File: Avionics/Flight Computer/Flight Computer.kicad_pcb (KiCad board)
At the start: 4 copper layers, 50 x 40 mm, 177 parts, among them J1 ERF8-040-05.0-S-DV-K, J2 ERF8-040-05.0-S-DV-K, J3 473460001, J4 734120110, J5 0734120110, J6 734120110, U1 CC1310F128RGZR, U12 ATSAME70Q21A-AN, U2 CC1190RGVR, U3 CC2650F128RGZR, U4 CC2592RGVR, U5 MPU-9250, U7 LPS25HB, U8 MAX17243, U9 MAX-M8W, Y1 9HT11-32.768KDZB-T, Y2 7V-16.000MAHJ-T, Y3 XRCGB24M000F2P00R0, Y5 XRCGB24M000F2P00R0

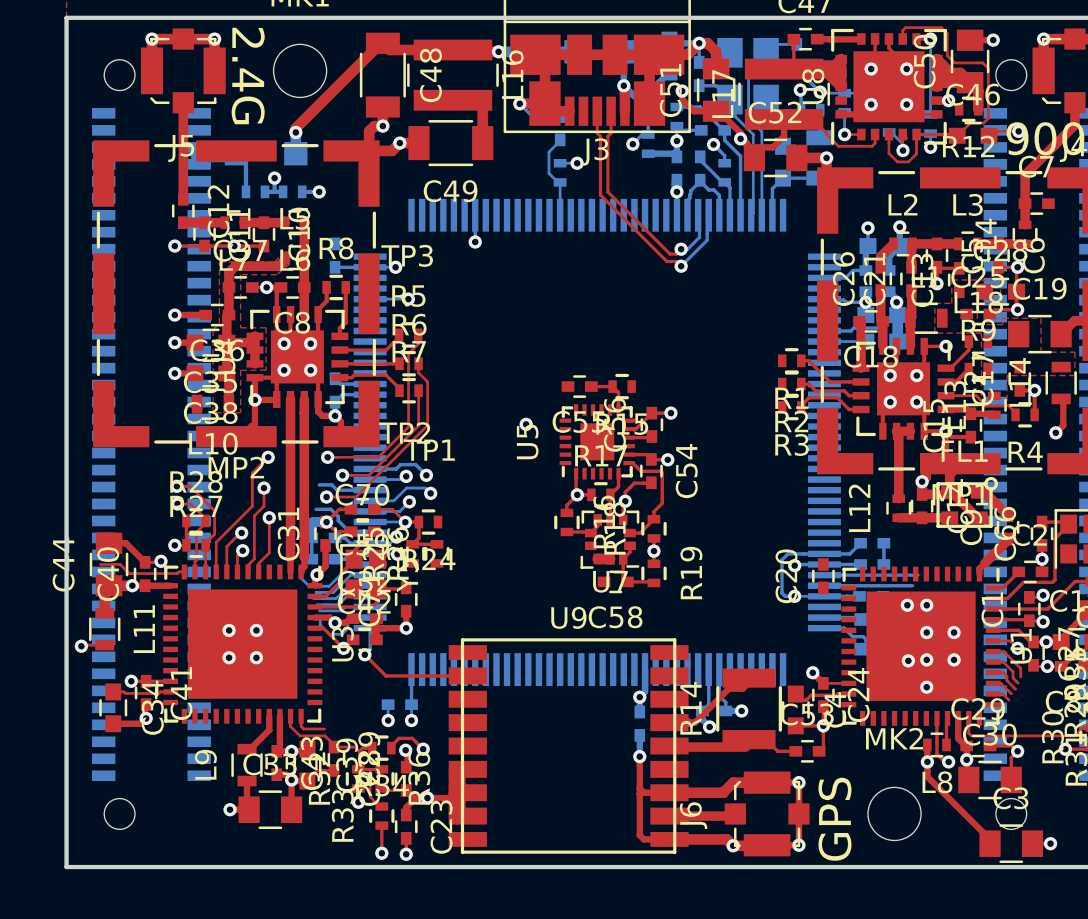
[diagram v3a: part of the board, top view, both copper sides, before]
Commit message: Continuing to route out MCU signals.
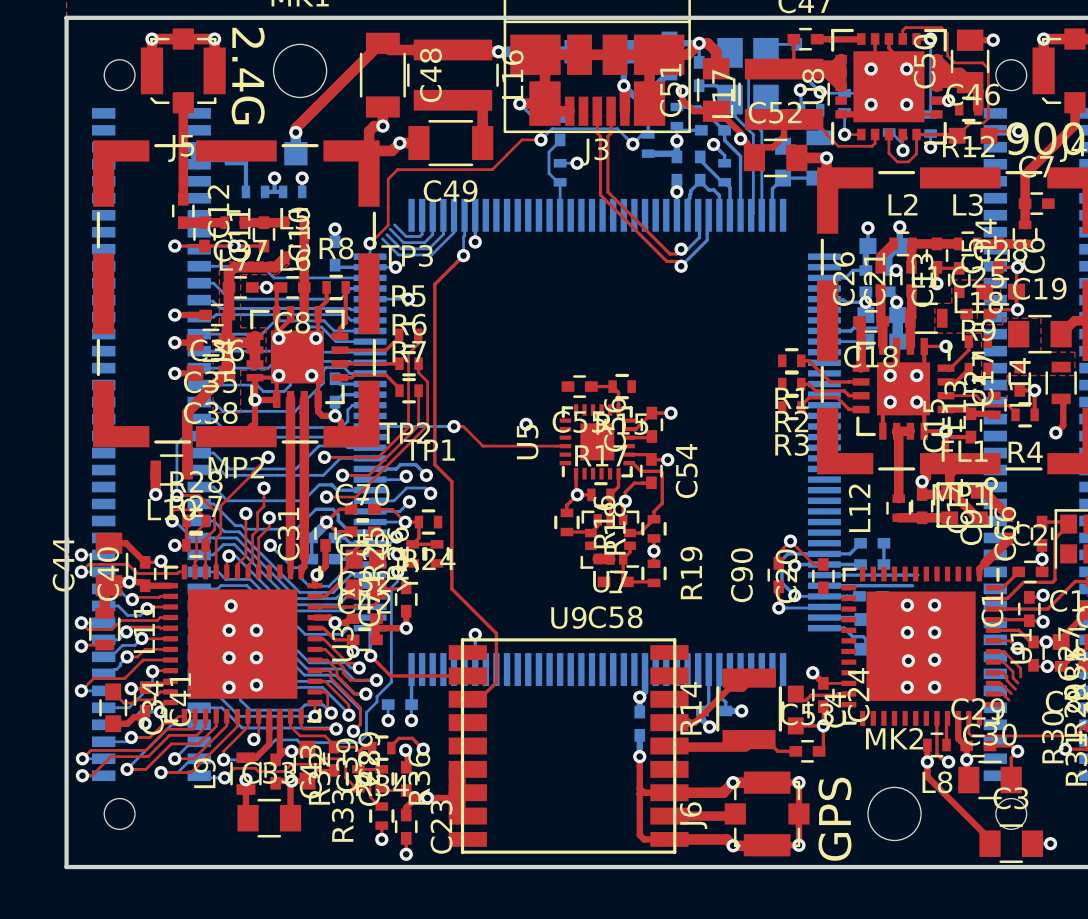
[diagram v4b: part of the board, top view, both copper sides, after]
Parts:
- added C90: 0.1u, Capacitors_SMD:C_0402, F.Cu at (83.5, 111.2)
- moved L10 3.66 mm to (55.0, 106.3)
- moved C43 0.40 mm to (59.9, 120.5)
- moved L9 0.40 mm to (58.5, 120.6)
- moved C33 0.40 mm to (59.6, 122.7)
- moved C41 0.30 mm to (53.7, 117.1)
- moved C77 0.10 mm to (62.6, 96.1)
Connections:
- J1 pad 11: Net-(J1-Pad11) -> /Connectors/PD9
- J1 pad 13: Net-(J1-Pad13) -> /Connectors/PC18
- J1 pad 15: Net-(J1-Pad15) -> /Connectors/PA28
- J1 pad 17: Net-(J1-Pad17) -> /Connectors/PD8
- J1 pad 19: Net-(J1-Pad19) -> /Connectors/PD15
- J1 pad 21: Net-(J1-Pad21) -> /Connectors/PB4
- J1 pad 23: Net-(J1-Pad23) -> /Connectors/PC17
- J1 pad 25: Net-(J1-Pad25) -> /Connectors/PA0
- J1 pad 27: Net-(J1-Pad27) -> /Connectors/PD10
- J1 pad 29: Net-(J1-Pad29) -> /Connectors/PC16
- J1 pad 31: Net-(J1-Pad31) -> /Connectors/PA1
- J1 pad 33: Net-(J1-Pad33) -> /Connectors/PD11
- J1 pad 35: Net-(J1-Pad35) -> /Connectors/PC14
- J1 pad 37: Net-(J1-Pad37) -> /Connectors/PC11
- J1 pad 39: Net-(J1-Pad39) -> /CPU-SDA
- J1 pad 41: Net-(J1-Pad41) -> /Connectors/PC10
- J1 pad 43: Net-(J1-Pad43) -> /Connectors/PB7
- J1 pad 45: Net-(J1-Pad45) -> /Connectors/PC9
- J1 pad 47: Net-(J1-Pad47) -> /Connectors/PC8
- J1 pad 49: Net-(J1-Pad49) -> /Connectors/PD16
- J1 pad 51: Net-(J1-Pad51) -> /CPU-SCK
- J1 pad 53: Net-(J1-Pad53) -> /Connectors/PC28
- J1 pad 54: Net-(J1-Pad54) -> /Connectors/PB6
- J1 pad 55: Net-(J1-Pad55) -> /Connectors/PD17
- J1 pad 56: Net-(J1-Pad56) -> /Connectors/2.4-DIO-7
- J1 pad 57: Net-(J1-Pad57) -> /Connectors/2.4-ADIO-30
- J1 pad 58: Net-(J1-Pad58) -> /Connectors/2.4-DIO-8
- J1 pad 59: Net-(J1-Pad59) -> /Connectors/2.4-ADIO-29
- J1 pad 60: Net-(J1-Pad60) -> /Connectors/2.4-DIO-9
- J1 pad 61: Net-(J1-Pad61) -> /Connectors/2.4-ADIO-28
- J1 pad 62: Net-(J1-Pad62) -> /Connectors/2.4-DIO-10
- J1 pad 63: Net-(J1-Pad63) -> /Connectors/2.4-ADIO-27
- J1 pad 64: Net-(J1-Pad64) -> /Connectors/2.4-DIO-11
- J1 pad 65: Net-(J1-Pad65) -> /Connectors/2.4-ADIO-26
- J1 pad 66: Net-(J1-Pad66) -> /Connectors/2.4-DIO-12
- J1 pad 67: Net-(J1-Pad67) -> /Connectors/2.4-ADIO-25
- J1 pad 68: Net-(J1-Pad68) -> /Connectors/2.4-DIO-13
- J1 pad 69: Net-(J1-Pad69) -> /Connectors/2.4-ADIO-24
- J1 pad 70: Net-(J1-Pad70) -> /Connectors/2.4-DIO-14
- J1 pad 71: Net-(J1-Pad71) -> /Connectors/2.4-ADIO-23
- J1 pad 72: Net-(J1-Pad72) -> /Connectors/2.4-DIO-15
- J1 pad 73: Net-(J1-Pad73) -> /Connectors/2.4-DIO-18
- J1 pad 74: Net-(J1-Pad74) -> /2.4-TMSC
- J1 pad 75: Net-(J1-Pad75) -> /Connectors/2.4-DIO-19
- J1 pad 76: Net-(J1-Pad76) -> /2.4-TCKC
- J1 pad 77: Net-(J1-Pad77) -> /Connectors/2.4-DIO-20
- J1 pad 78: Net-(J1-Pad78) -> /Connectors/2.4-DIO-16
- J1 pad 79: Net-(J1-Pad79) -> /2.4_RESET_EXT
- J1 pad 80: Net-(J1-Pad80) -> /Connectors/2.4-DIO-17
- J1 pad 9: Net-(J1-Pad9) -> /Connectors/PB5
- U12 pad 100: /GNC_Processor/PC16 -> /Connectors/PC16
- U12 pad 101: /GNC_Processor/PD10 -> /Connectors/PD10
- U12 pad 103: /GNC_Processor/PC17 -> /Connectors/PC17
- U12 pad 105: /GNC_Processor/PB4 -> /Connectors/PB4
- U12 pad 106: /GNC_Processor/PD15 -> /Connectors/PD15
- U12 pad 109: /GNC_Processor/PB5 -> /Connectors/PB5
- U12 pad 110: /GNC_Processor/PD9 -> /Connectors/PD9
- U12 pad 111: /GNC_Processor/PC18 -> /Connectors/PC18
- U12 pad 112: /GNC_Processor/PA28 -> /Connectors/PA28
- U12 pad 113: /GNC_Processor/PD8 -> /Connectors/PD8
- U12 pad 74: /GNC_Processor/PD17 -> /Connectors/PD17
- U12 pad 76: /GNC_Processor/PC28 -> /Connectors/PC28
- U12 pad 78: /GNC_Processor/PD16 -> /Connectors/PD16
- U12 pad 79: /GNC_Processor/PB6 -> /Connectors/PB6
- U12 pad 82: /GNC_Processor/PC8 -> /Connectors/PC8
- U12 pad 86: /GNC_Processor/PC9 -> /Connectors/PC9
- U12 pad 89: /GNC_Processor/PB7 -> /Connectors/PB7
- U12 pad 90: /GNC_Processor/PC10 -> /Connectors/PC10
- U12 pad 94: /GNC_Processor/PC11 -> /Connectors/PC11
- U12 pad 97: /GNC_Processor/PC14 -> /Connectors/PC14
- U12 pad 98: /GNC_Processor/PD11 -> /Connectors/PD11
- U3 pad 12: /2.4 GHz Radio/DIO-7 -> /Connectors/2.4-DIO-7
- U3 pad 14: /2.4 GHz Radio/DIO-8 -> /Connectors/2.4-DIO-8
- U3 pad 15: /2.4 GHz Radio/DIO-9 -> /Connectors/2.4-DIO-9
- U3 pad 16: /2.4 GHz Radio/DIO-10 -> /Connectors/2.4-DIO-10
- U3 pad 17: /2.4 GHz Radio/DIO-11 -> /Connectors/2.4-DIO-11
- U3 pad 18: /2.4 GHz Radio/DIO-12 -> /Connectors/2.4-DIO-12
- U3 pad 19: /2.4 GHz Radio/DIO-13 -> /Connectors/2.4-DIO-13
- U3 pad 20: /2.4 GHz Radio/DIO-14 -> /Connectors/2.4-DIO-14
- U3 pad 21: /2.4 GHz Radio/DIO-15 -> /Connectors/2.4-DIO-15
- U3 pad 26: /2.4 GHz Radio/DIO-16 -> /Connectors/2.4-DIO-16
- U3 pad 27: /2.4 GHz Radio/DIO-17 -> /Connectors/2.4-DIO-17
- U3 pad 28: /2.4 GHz Radio/DIO-18 -> /Connectors/2.4-DIO-18
- U3 pad 29: /2.4 GHz Radio/DIO-19 -> /Connectors/2.4-DIO-19
- U3 pad 30: /2.4 GHz Radio/DIO-20 -> /Connectors/2.4-DIO-20
- U3 pad 36: /2.4 GHz Radio/ADIO-23 -> /Connectors/2.4-ADIO-23
- U3 pad 37: /2.4 GHz Radio/ADIO-24 -> /Connectors/2.4-ADIO-24
- U3 pad 38: /2.4 GHz Radio/ADIO-25 -> /Connectors/2.4-ADIO-25
- U3 pad 39: /2.4 GHz Radio/ADIO-26 -> /Connectors/2.4-ADIO-26
- U3 pad 40: /2.4 GHz Radio/ADIO-27 -> /Connectors/2.4-ADIO-27
- U3 pad 41: /2.4 GHz Radio/ADIO-28 -> /Connectors/2.4-ADIO-28
- U3 pad 42: /2.4 GHz Radio/ADIO-29 -> /Connectors/2.4-ADIO-29
- U3 pad 43: /2.4 GHz Radio/ADIO-30 -> /Connectors/2.4-ADIO-30
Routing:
- net /GPS/GPS-Rx: track 0.00 -> 25.5 mm, vias 0 -> 1
- net /2.4 GHz Radio/VDDS_CC2650: track 11.6 -> 33.9 mm
- net /CPU_RESET_2.4: track 0.00 -> 19.0 mm, vias 0 -> 2
- net /2.4G-Rx: track 1.10 -> 18.9 mm, vias 1 -> 2
- net /Connectors/PB6: track 0.00 -> 17.1 mm, vias 0 -> 2
- net /GNC_Processor/VBUS_DETECT: track 1.81 -> 18.6 mm, vias 1 -> 3
- net /2.4 GHz Radio/VDDR_CC2650: track 6.24 -> 22.5 mm
- net /Connectors/2.4-ADIO-29: track 0.00 -> 14.4 mm, vias 0 -> 1
- net /Connectors/2.4-ADIO-27: track 0.00 -> 14.4 mm, vias 0 -> 1
- net /Connectors/2.4-ADIO-28: track 0.00 -> 13.0 mm, vias 0 -> 1
- net /Connectors/2.4-ADIO-30: track 0.00 -> 12.3 mm, vias 0 -> 1
- net /CPU-SDA: track 5.31 -> 16.8 mm
- net GND: track 225.3 -> 236.5 mm, vias 78 -> 85
- net /Connectors/2.4-ADIO-26: track 0.00 -> 10.8 mm, vias 0 -> 1
- net /Connectors/2.4-DIO-18: track 0.00 -> 9.90 mm, vias 0 -> 1
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
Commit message: Did some more routing
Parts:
- moved C20 0.75 mm to (85.7, 110.5)
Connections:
- J1 pad 1: Net-(J1-Pad1) -> /Connectors/PC19
- J1 pad 10: Net-(J1-Pad10) -> /Connectors/PA31
- J1 pad 2: Net-(J1-Pad2) -> /Connectors/PC21
- J1 pad 3: Net-(J1-Pad3) -> /Connectors/PA30
- J1 pad 4: Net-(J1-Pad4) -> /Connectors/PD6
- J1 pad 6: Net-(J1-Pad6) -> /Connectors/PC20
- J1 pad 8: Net-(J1-Pad8) -> /Connectors/PD7
- U12 pad 116: /GNC_Processor/PA30 -> /Connectors/PA30
- U12 pad 117: /GNC_Processor/PC19 -> /Connectors/PC19
- U12 pad 118: /GNC_Processor/PA31 -> /Connectors/PA31
- U12 pad 119: /GNC_Processor/PD7 -> /Connectors/PD7
- U12 pad 120: /GNC_Processor/PC20 -> /Connectors/PC20
- U12 pad 121: /GNC_Processor/PD6 -> /Connectors/PD6
- U12 pad 122: /GNC_Processor/PC21 -> /Connectors/PC21
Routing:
- net Net-(C57-Pad1): track 23.0 -> 90.2 mm, vias 7 -> 10
- net /Connectors/PD6: track 0.00 -> 29.2 mm
- net /Connectors/PC20: track 0.00 -> 28.7 mm
- net /Connectors/PD7: track 0.00 -> 28.7 mm
- net /Connectors/PC21: track 0.00 -> 28.1 mm, vias 0 -> 2
- net /Connectors/PA31: track 0.00 -> 23.7 mm
- net /900MHz Radio/VDDS_CC1310: track 12.4 -> 36.0 mm
- net /Connectors/PC19: track 0.00 -> 16.5 mm
- net /Connectors/PA30: track 0.00 -> 16.0 mm
- net /900MHz Radio/VDDR_CC1310: track 10.1 -> 25.5 mm
- net /GNC_Processor/GPS-~RESET: track 0.00 -> 12.1 mm, vias 0 -> 1
- net /Connectors/PB5: track 0.00 -> 11.5 mm
- net /Connectors/PD9: track 2.47 -> 13.0 mm
- net /Connectors/PC18: track 3.33 -> 13.4 mm
- net /Connectors/PA28: track 4.12 -> 14.1 mm
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
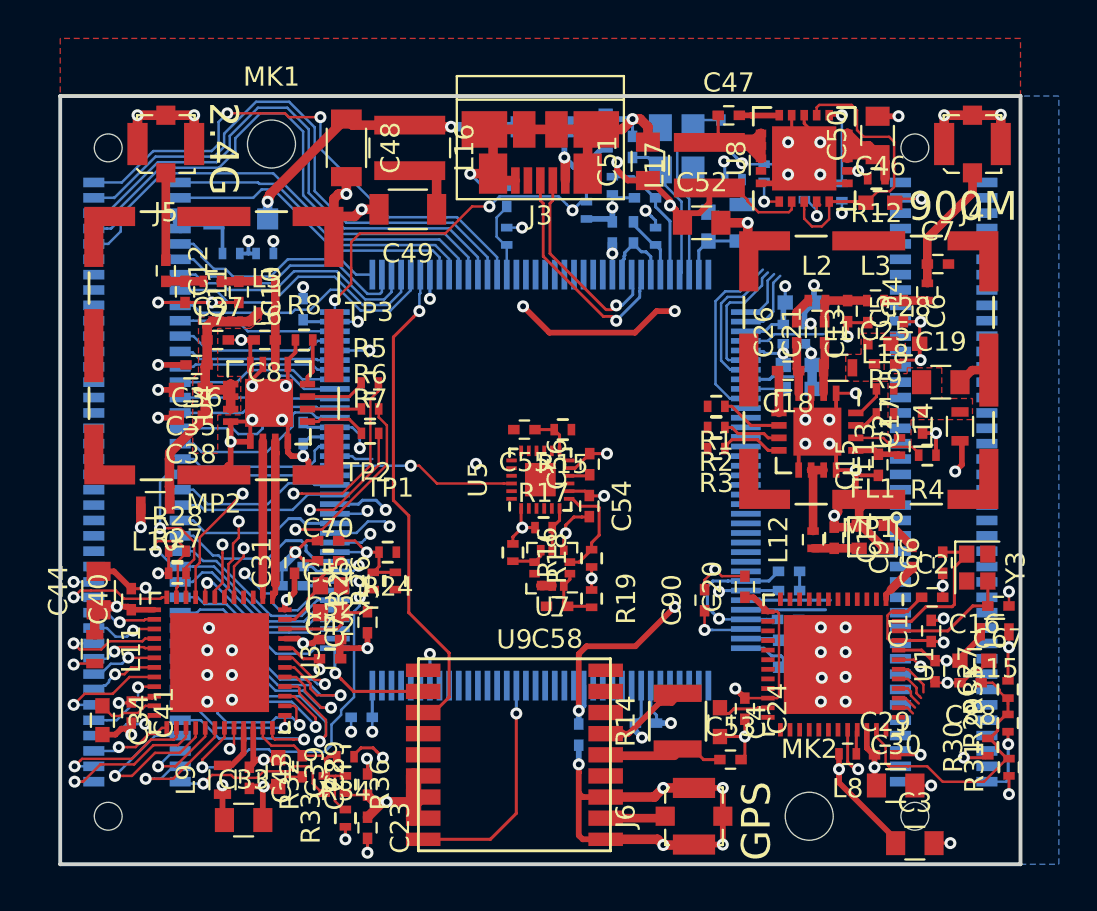
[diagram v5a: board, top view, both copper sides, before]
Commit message: Additional routing
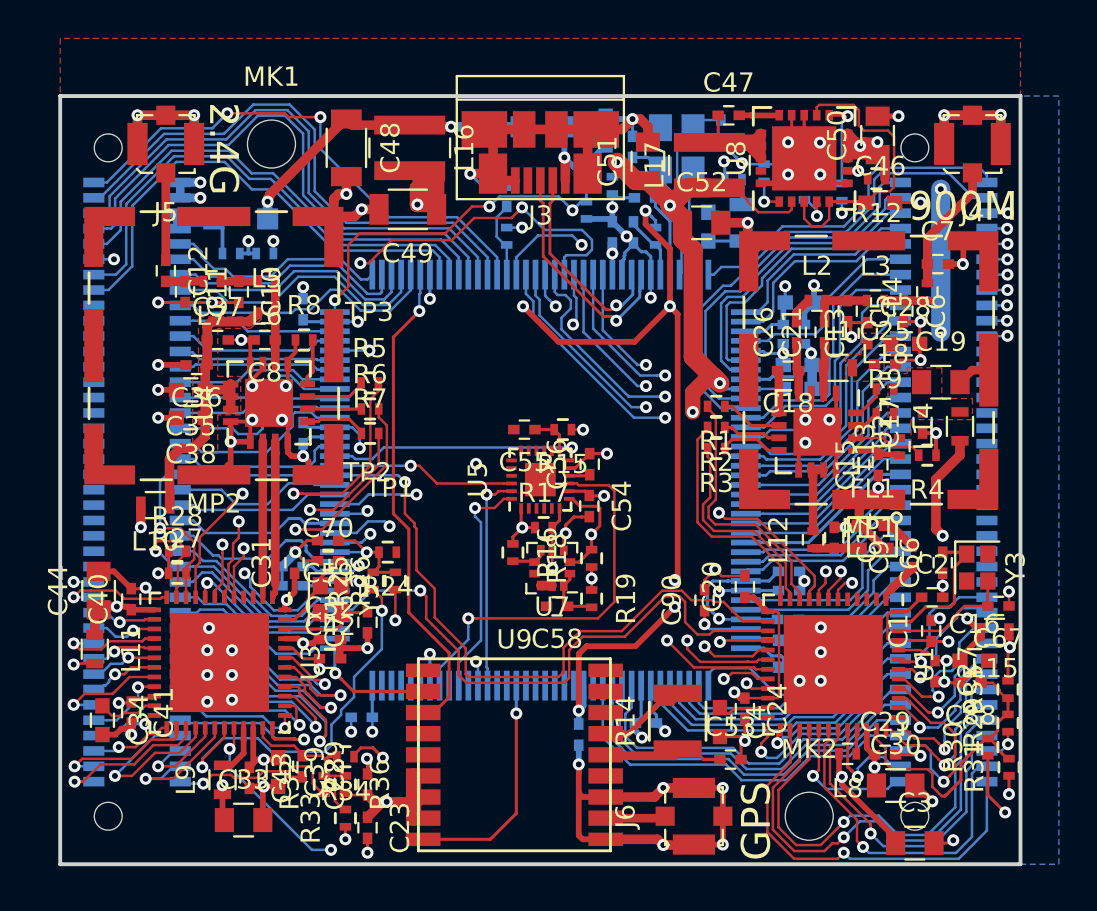
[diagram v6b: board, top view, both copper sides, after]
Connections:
- J1 pad 1: /Connectors/PC19 -> GND
- J1 pad 12: Net-(J1-Pad12) -> /Connectors/PA29
- J1 pad 14: Net-(J1-Pad14) -> /Connectors/PC19
- J1 pad 16: Net-(J1-Pad16) -> /Connectors/PA30
- J1 pad 3: /Connectors/PA30 -> GND
- J2 pad 1: Net-(J2-Pad1) -> /Connectors/PB13
- J2 pad 10: Net-(J2-Pad10) -> /Connectors/PD31
- J2 pad 11: Net-(J2-Pad11) -> /Connectors/PC25
- J2 pad 12: Net-(J2-Pad12) -> /Connectors/PE0
- J2 pad 13: Net-(J2-Pad13) -> /Connectors/PD1
- J2 pad 14: Net-(J2-Pad14) -> /Connectors/PC27
- J2 pad 15: Net-(J2-Pad15) -> /Connectors/PD2
- J2 pad 16: Net-(J2-Pad16) -> /Connectors/PC26
- J2 pad 17: Net-(J2-Pad17) -> /Connectors/PD3
- J2 pad 18: Net-(J2-Pad18) -> /Connectors/PC31
- J2 pad 19: Net-(J2-Pad19) -> /Connectors/PD4
- J2 pad 2: Net-(J2-Pad2) -> /Connectors/PE3
- J2 pad 20: Net-(J2-Pad20) -> /Connectors/PC30
- J2 pad 21: Net-(J2-Pad21) -> /Connectors/PD5
- J2 pad 22: Net-(J2-Pad22) -> /Connectors/PC29
- J2 pad 24: Net-(J2-Pad24) -> /Connectors/PC12
- J2 pad 26: Net-(J2-Pad26) -> /Connectors/PC15
- J2 pad 28: Net-(J2-Pad28) -> /Connectors/PC13
- J2 pad 3: Net-(J2-Pad3) -> /Connectors/PC0
- J2 pad 30: Net-(J2-Pad30) -> /Connectors/PB1
- J2 pad 32: Net-(J2-Pad32) -> /Connectors/PB0
- J2 pad 34: Net-(J2-Pad34) -> /Connectors/PA20
- J2 pad 36: Net-(J2-Pad36) -> /Connectors/PA19
- J2 pad 38: Net-(J2-Pad38) -> /Connectors/PA18
- J2 pad 4: Net-(J2-Pad4) -> /Connectors/PE2
- J2 pad 40: Net-(J2-Pad40) -> /Connectors/PA17
- J2 pad 42: Net-(J2-Pad42) -> /Connectors/PB2
- J2 pad 44: Net-(J2-Pad44) -> /Connectors/PE4
- J2 pad 46: Net-(J2-Pad46) -> /Connectors/PE5
- J2 pad 48: Net-(J2-Pad48) -> /Connectors/PB3
- J2 pad 5: Net-(J2-Pad5) -> /Connectors/PC22
- J2 pad 50: Net-(J2-Pad50) -> /Connectors/PA21
- J2 pad 52: Net-(J2-Pad52) -> /Connectors/PA22
- J2 pad 54: Net-(J2-Pad54) -> /Connectors/PC1
- J2 pad 55: Net-(J2-Pad55) -> /Connectors/900-ADIO-30
- J2 pad 56: Net-(J2-Pad56) -> /Connectors/PC2
- J2 pad 57: Net-(J2-Pad57) -> /Connectors/900-ADIO-29
- J2 pad 58: Net-(J2-Pad58) -> /Connectors/PC3
- J2 pad 59: Net-(J2-Pad59) -> /Connectors/900-ADIO-28
- J2 pad 6: Net-(J2-Pad6) -> /Connectors/PE1
- J2 pad 60: Net-(J2-Pad60) -> /Connectors/PC4
- J2 pad 61: Net-(J2-Pad61) -> /Connectors/900-ADIO-27
- J2 pad 62: Net-(J2-Pad62) -> /Connectors/PA13
- J2 pad 63: /Connectors/900-ADIO-30 -> /Connectors/900-ADIO-25
- J2 pad 64: Net-(J2-Pad64) -> /900-TCKC
- J2 pad 65: /Connectors/900-ADIO-29 -> /Connectors/900-ADIO-24
- J2 pad 66: Net-(J2-Pad66) -> /900-TMSC
- J2 pad 67: /Connectors/900-ADIO-28 -> /Connectors/900-ADIO-23
- J2 pad 68: Net-(J2-Pad68) -> /Connectors/PA16
- J2 pad 69: /Connectors/900-ADIO-26 -> /Connectors/900-DIO-18
- J2 pad 7: Net-(J2-Pad7) -> /Connectors/PC23
- J2 pad 70: Net-(J2-Pad70) -> /Connectors/PA23
- J2 pad 71: /Connectors/900-ADIO-23 -> /Connectors/900-DIO-17
- J2 pad 72: Net-(J2-Pad72) -> /Connectors/PD27
- J2 pad 73: /Connectors/900-ADIO-24 -> /Connectors/900-DIO-21
- J2 pad 74: Net-(J2-Pad74) -> /Connectors/PC7
- J2 pad 75: /Connectors/900-ADIO-25 -> /900_RESET_EXT
- J2 pad 76: Net-(J2-Pad76) -> /Connectors/900-ADIO-26
- J2 pad 77: /Connectors/900-ADIO-27 -> /Connectors/900-DIO-20
- J2 pad 78: Net-(J2-Pad78) -> /Connectors/900-DIO-22
- J2 pad 79: /900_RESET_EXT -> /Connectors/900-DIO-16
- J2 pad 8: Net-(J2-Pad8) -> /Connectors/PD0
- J2 pad 80: Net-(J2-Pad80) -> /Connectors/900-DIO-19
- J2 pad 9: Net-(J2-Pad9) -> /Connectors/PC24
- U1 pad 26: /900MHz Radio/DIO-16 -> /Connectors/900-DIO-16
- U1 pad 27: /900MHz Radio/DIO-17 -> /Connectors/900-DIO-17
- U1 pad 28: /900MHz Radio/DIO-18 -> /Connectors/900-DIO-18
- U1 pad 29: /900MHz Radio/DIO-19 -> /Connectors/900-DIO-19
- U1 pad 30: /900MHz Radio/DIO-20 -> /Connectors/900-DIO-20
- U1 pad 31: /900MHz Radio/DIO-21 -> /Connectors/900-DIO-21
- U1 pad 32: /900MHz Radio/DIO-22 -> /Connectors/900-DIO-22
- U12 pad 1: /GNC_Processor/PD0 -> /Connectors/PD0
- U12 pad 10: /GNC_Processor/PE3 -> /Connectors/PE3
- U12 pad 11: /GNC_Processor/PC0 -> /Connectors/PC0
- U12 pad 12: /GNC_Processor/PC27 -> /Connectors/PC27
- U12 pad 124: /GNC_Processor/PC22 -> /Connectors/PC22
- U12 pad 125: /GNC_Processor/PD5 -> /Connectors/PD5
- U12 pad 126: /GNC_Processor/PD4 -> /Connectors/PD4
- U12 pad 127: /GNC_Processor/PC23 -> /Connectors/PC23
- U12 pad 128: /GNC_Processor/PD3 -> /Connectors/PD3
- U12 pad 129: /GNC_Processor/PA29 -> /Connectors/PA29
- U12 pad 13: /GNC_Processor/PC26 -> /Connectors/PC26
- U12 pad 130: /GNC_Processor/PC24 -> /Connectors/PC24
- U12 pad 131: /GNC_Processor/PD2 -> /Connectors/PD2
- U12 pad 132: /GNC_Processor/PD1 -> /Connectors/PD1
- U12 pad 133: /GNC_Processor/PC25 -> /Connectors/PC25
- U12 pad 14: /GNC_Processor/PC31 -> /Connectors/PC31
- U12 pad 15: /GNC_Processor/PC30 -> /Connectors/PC30
- U12 pad 16: /GNC_Processor/PC29 -> /Connectors/PC29
- U12 pad 17: /GNC_Processor/PC12 -> /Connectors/PC12
- U12 pad 18: /GNC_Processor/PC15 -> /Connectors/PC15
- U12 pad 19: /GNC_Processor/PC13 -> /Connectors/PC13
- U12 pad 20: /GNC_Processor/PB1 -> /Connectors/PB1
- U12 pad 21: /GNC_Processor/PB0 -> /Connectors/PB0
- U12 pad 22: /GNC_Processor/PA20 -> /Connectors/PA20
- U12 pad 23: /GNC_Processor/PA19 -> /Connectors/PA19
- U12 pad 24: /GNC_Processor/PA18 -> /Connectors/PA18
- U12 pad 25: /GNC_Processor/PA17 -> /Connectors/PA17
- U12 pad 26: /GNC_Processor/PB2 -> /Connectors/PB2
- U12 pad 27: /GNC_Processor/PE4 -> /Connectors/PE4
- U12 pad 28: /GNC_Processor/PE5 -> /Connectors/PE5
- U12 pad 31: /GNC_Processor/PB3 -> /Connectors/PB3
- U12 pad 32: /GNC_Processor/PA21 -> /Connectors/PA21
- U12 pad 37: /GNC_Processor/PA22 -> /Connectors/PA22
- U12 pad 38: /GNC_Processor/PC1 -> /Connectors/PC1
- U12 pad 39: /GNC_Processor/PC2 -> /Connectors/PC2
- U12 pad 4: /GNC_Processor/PE0 -> /Connectors/PE0
- U12 pad 40: /GNC_Processor/PC3 -> /Connectors/PC3
- U12 pad 41: /GNC_Processor/PC4 -> /Connectors/PC4
- U12 pad 42: /GNC_Processor/PA13 -> /Connectors/PA13
- U12 pad 45: /GNC_Processor/PA16 -> /Connectors/PA16
- U12 pad 46: /GNC_Processor/PA23 -> /Connectors/PA23
- U12 pad 47: /GNC_Processor/PD27 -> /Connectors/PD27
- U12 pad 48: /GNC_Processor/PC7 -> /Connectors/PC7
- U12 pad 6: /GNC_Processor/PE1 -> /Connectors/PE1
- U12 pad 7: /GNC_Processor/PE2 -> /Connectors/PE2
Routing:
- net /900_RESET_2.4: track 2.47 -> 53.4 mm, vias 2 -> 3
- net +3V3: track 59.5 -> 96.5 mm, vias 19 -> 24
- net /Connectors/PD5: track 0.00 -> 35.7 mm, vias 0 -> 2
- net /Connectors/PC22: track 0.00 -> 34.9 mm, vias 0 -> 2
- net /Connectors/PD4: track 0.00 -> 34.7 mm, vias 0 -> 2
- net /CPU-SDA: track 16.8 -> 51.0 mm, vias 1 -> 2
- net /Connectors/PD3: track 0.00 -> 34.1 mm, vias 0 -> 2
- net /Connectors/PD2: track 0.00 -> 32.0 mm, vias 0 -> 2
- net /Connectors/PA29: track 0.00 -> 30.9 mm, vias 0 -> 3
- net /CPU-SCK: track 16.0 -> 46.6 mm, vias 1 -> 2
- net /Connectors/PD1: track 0.00 -> 30.5 mm, vias 0 -> 2
- net /Connectors/PC24: track 0.00 -> 30.3 mm, vias 0 -> 2
- net /Connectors/PC23: track 0.00 -> 30.0 mm, vias 0 -> 2
- net /Connectors/PC25: track 0.00 -> 29.4 mm, vias 0 -> 2
- net /Connectors/PC0: track 0.00 -> 26.2 mm
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- added copper zone on In2.Cu, net Net-(C49-Pad1)
